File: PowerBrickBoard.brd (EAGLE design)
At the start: 60.3 x 40 mm, 5 parts

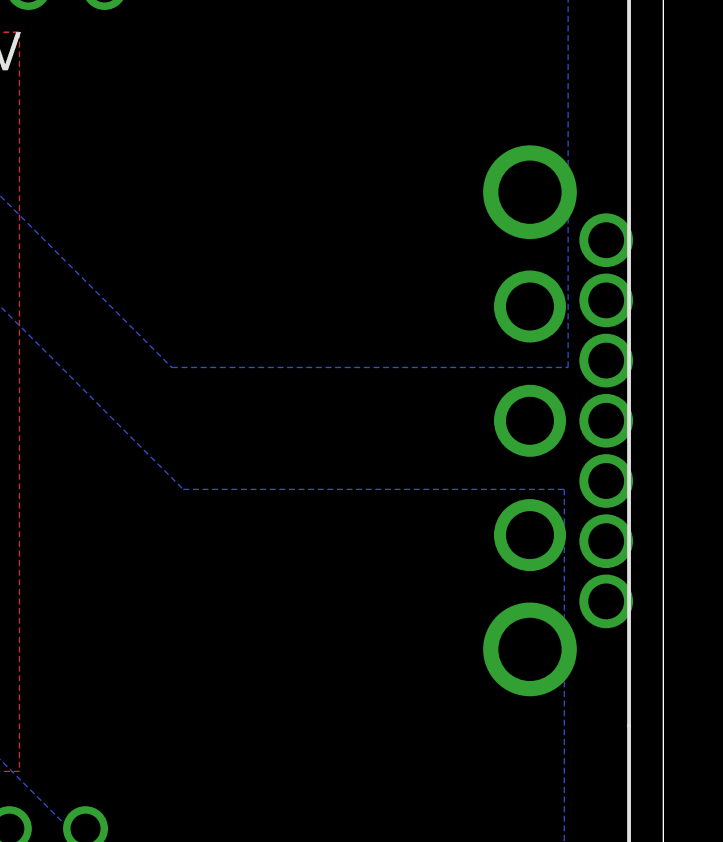
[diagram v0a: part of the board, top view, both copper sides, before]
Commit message: added LED
added LED between 12V and GND
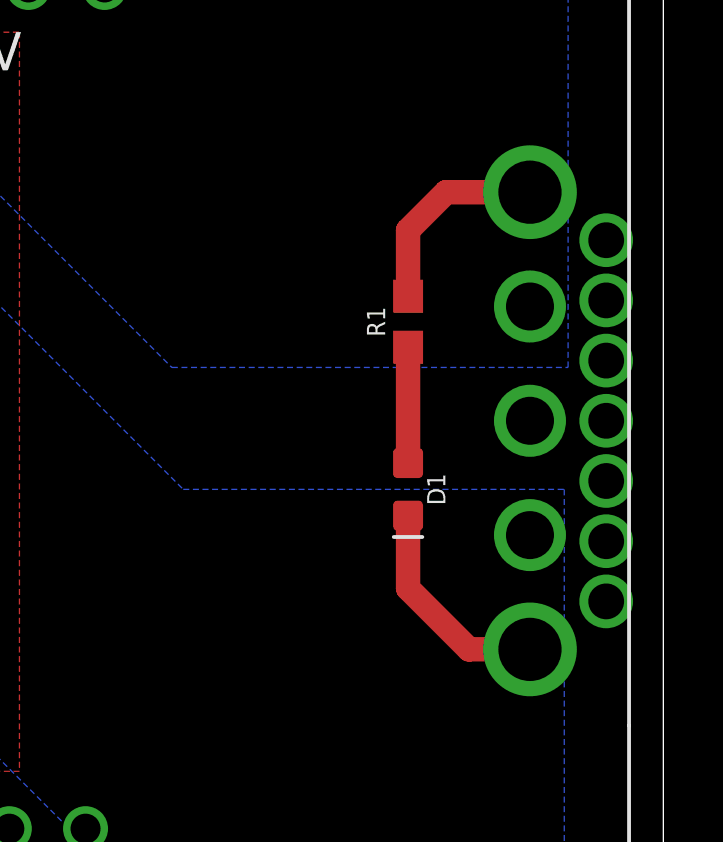
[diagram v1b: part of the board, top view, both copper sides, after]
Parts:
- added D1: (no value), SparkFun-LED:LED-0603
- added R1: 470, SparkFun-Resistors:0603
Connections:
- new net N$1: D1.A, R1.1
- net +12V: now also R1.2
- net GND: now also D1.C
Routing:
- net GND: track 0.00 -> 7.33 mm
- net +12V: track 0.00 -> 6.79 mm
- net N$1: track 0.00 -> 3.86 mm
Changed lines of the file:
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@@
 <layer number="112" name="tSilk" color="7" fill="1" visible="yes" active="yes"/>
 <layer number="113" name="IDFDebug" color="7" fill="1" visible="yes" active="yes"/>
+<layer number="114" name="Badge_Outline" color="7" fill="1" visible="yes" active="yes"/>
+<layer number="115" name="ReferenceISLANDS" color="7" fill="1" visible="yes" active="yes"/>
 <layer number="116" name="Patch_BOT" color="9" fill="4" visible="yes" active="yes"/>
 <layer number="118" name="Rect_Pads" color="7" fill="1" visible="yes" active="yes"/>
@@
 <layer number="230" name="230bmp" color="7" fill="1" visible="yes" active="yes"/>
 <layer number="231" name="231bmp" color="7" fill="1" visible="yes" active="yes"/>
+<layer number="232" name="Eagle3D_PG2" color="7" fill="1" visible="yes" active="yes"/>
+<layer number="233" name="Eagle3D_PG3" color="7" fill="1" visible="yes" active="yes"/>
 <layer number="248" name="Housing" color="7" fill="1" visible="yes" active="yes"/>
 <layer number="249" name="Edge" color="7" fill="1" visible="yes" active="yes"/>
@@
 <element name="U$4" library="UCM1H331MNL1GS" package="UCM1H331MNL1GS" value="330 uF" x="28.9919375" y="23.41605625" rot="R270"/>
 <element name="U$5" library="UCM1H331MNL1GS" package="UCM1H331MNL1GS" value="330 uF" x="14.068" y="24.996"/>
+<element name="D1" library="SparkFun-LED" library_urn="urn:adsk.eagle:library:529" package="LED-0603" package3d_urn="urn:adsk.eagle:package:39354/1" value="" x="51.816" y="17.78" rot="R270">
+<attribute name="NAME" x="52.451" y="17.78" size="0.6096" layer="25" font="vector" ratio="20" rot="R270" align="bottom-center"/>
+<attribute name="VALUE" x="51.181" y="17.78" size="0.6096" layer="27" font="vector" ratio="20" rot="R270" align="top-center"/>
+</element>
+<element name="R1" library="SparkFun-Resistors" library_urn="urn:adsk.eagle:library:532" package="0603" package3d_urn="urn:adsk.eagle:package:39650/1" value=" 470" x="51.816" y="23.368" rot="R90">
+<attribute name="NAME" x="51.054" y="23.368" size="0.6096" layer="25" font="vector" ratio="20" rot="R90" align="bottom-center"/>
+<attribute name="PROD_ID" value=" " x="51.816" y="23.368" size="1.778" layer="27" rot="R90" display="off"/>
+<attribute name="VALUE" x="52.578" y="23.368" size="0.6096" layer="27" font="vector" ratio="20" rot="R90" align="top-center"/>
+</element>
 </elements>
 <signals>
@@
 <vertex x="57.15" y="38.354"/>
 </polygon>
+<contactref element="R1" pad="2"/>
+<wire x1="55.88" y1="27.686" x2="53.086" y2="27.686" width="0.8128" layer="1"/>
+<wire x1="53.086" y1="27.686" x2="51.816" y2="26.416" width="0.8128" layer="1"/>
+<wire x1="51.816" y1="26.416" x2="51.816" y2="24.218" width="0.8128" layer="1"/>
 </signal>
 <signal name="+48V">
@@
 <vertex x="29.21" y="32.893"/>
 </polygon>
+<contactref element="D1" pad="C"/>
+<wire x1="51.816" y1="16.903" x2="51.816" y2="14.478" width="0.8128" layer="1"/>
+<wire x1="51.816" y1="14.478" x2="53.848" y2="12.446" width="0.8128" layer="1"/>
+<wire x1="53.848" y1="12.446" x2="55.88" y2="12.446" width="0.8128" layer="1"/>
 </signal>
 <signal name="48V_GND">
@@
 </polygon>
 </signal>
+<signal name="N$1">
+<contactref element="D1" pad="A"/>
+<contactref element="R1" pad="1"/>
+<wire x1="51.816" y1="22.518" x2="51.816" y2="18.657" width="0.8128" layer="1"/>
+</signal>
 </signals>
 <mfgpreviewcolors>
@@
 which will not be processed correctly with this version.
 </note>
+<note version="8.2" severity="warning">
+Since Version 8.2, EAGLE supports online libraries. The ids
+of those online libraries will not be understood (or retained)
+with this version.
+</note>
+<note version="8.3" severity="warning">
+Since Version 8.3, EAGLE supports URNs for individual library
+assets (packages, symbols, and devices). The URNs of those assets
+will not be understood (or retained) with this version.
+</note>
+<note version="8.3" severity="warning">
+Since Version 8.3, EAGLE supports the association of 3D packages
+with devices in libraries, schematics, and board files. Those 3D
+packages will not be understood (or retained) with this version.
+</note>
 </compatibility>

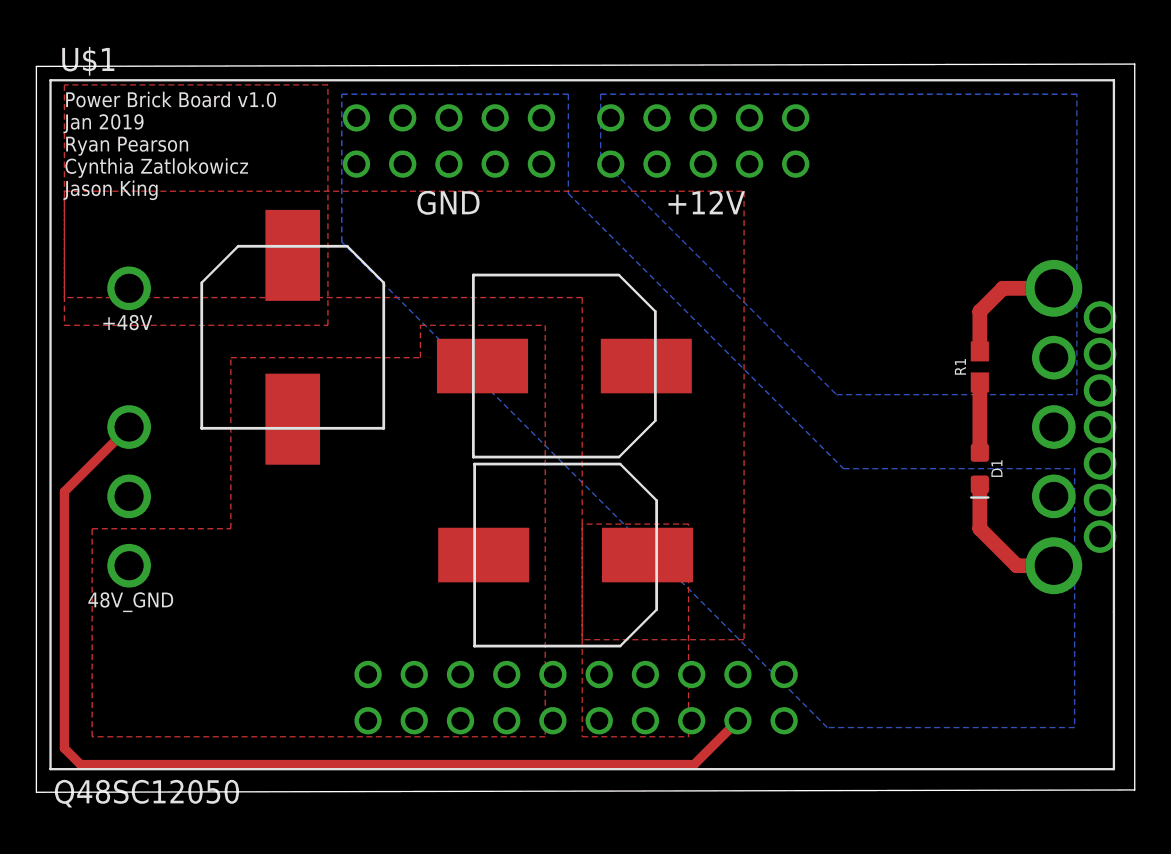
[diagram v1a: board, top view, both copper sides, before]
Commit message: added silkscreen
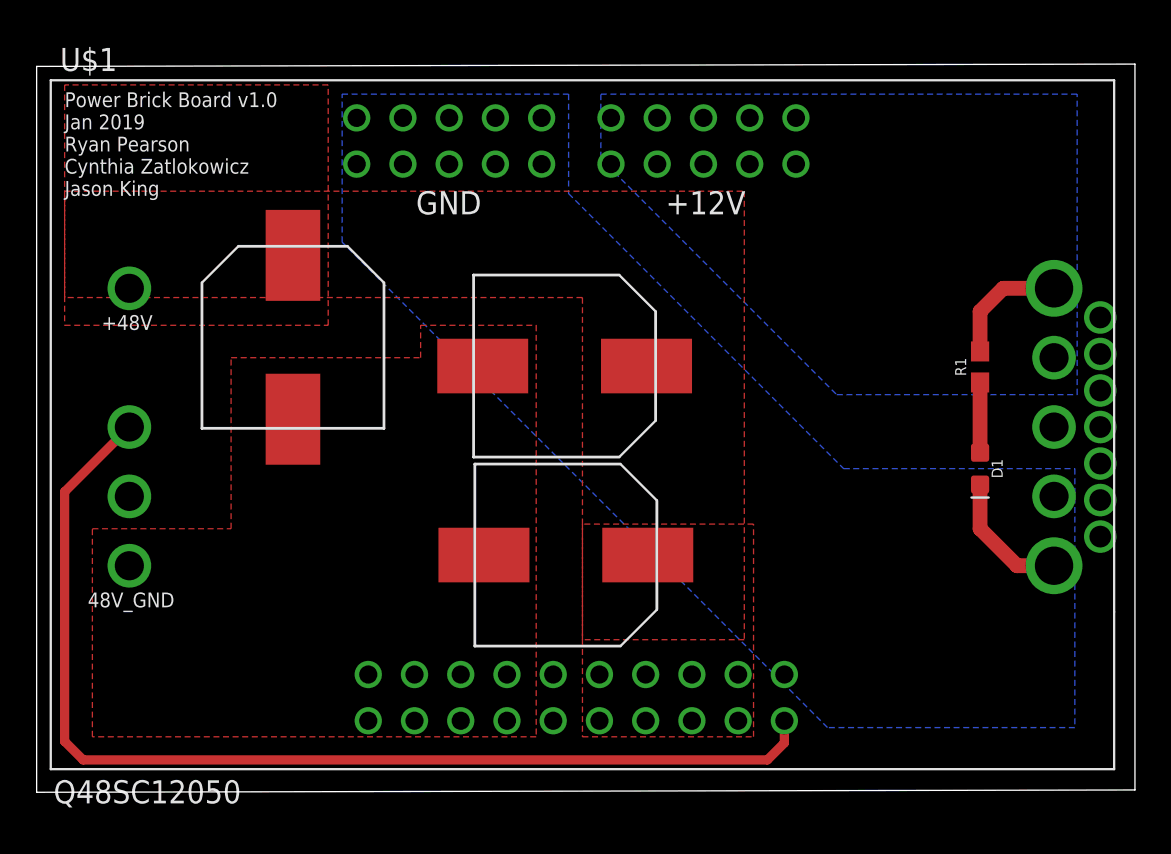
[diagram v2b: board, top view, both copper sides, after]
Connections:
- net +48V: now also U$2.+48V5, U$2.+48V6, U$2.+48V7, U$2.+48V8
- net 48V_GND: now also U$2.48V_GND5, U$2.48V_GND6, U$2.48V_GND7, U$2.48V_GND8
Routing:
- net ON/OFF: track 57.5 -> 60.3 mm
